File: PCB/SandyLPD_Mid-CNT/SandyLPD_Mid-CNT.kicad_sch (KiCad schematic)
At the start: 24 parts

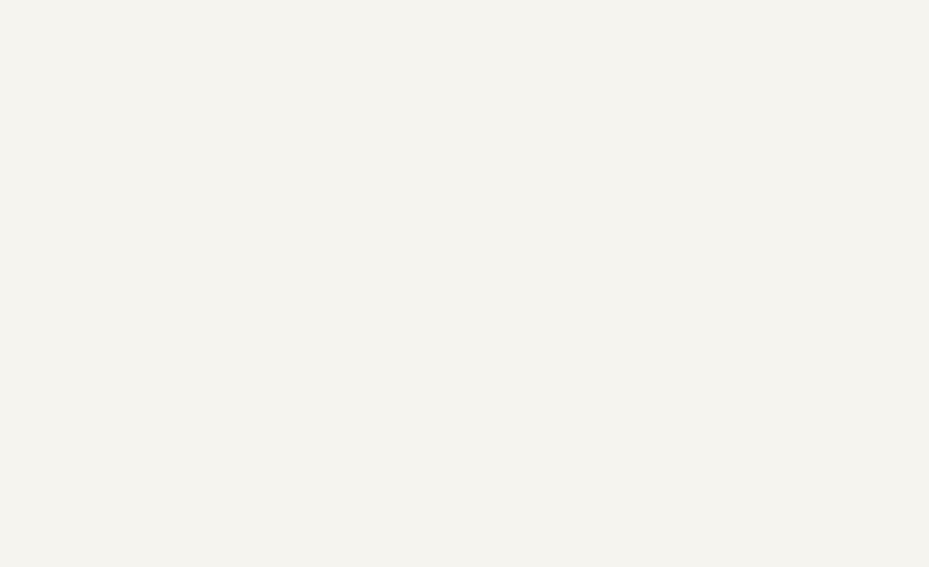
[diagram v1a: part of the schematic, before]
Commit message: Mid中央、配線やシルク調整中。
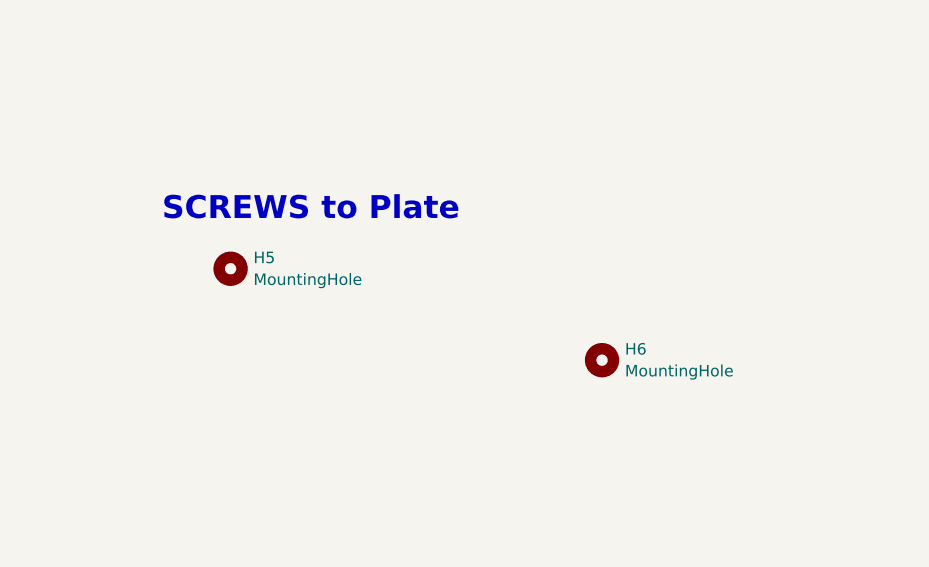
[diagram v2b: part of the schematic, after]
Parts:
- added H5, H6: MountingHole, locallib:MountingHole_M2_Through-hole_tap_THC-0.8-x-2, symbol Mechanical:MountingHole
- H1, H2, H3, H4: footprint locallib:MountingHole_1.8-2.2mm_M2_Pad_minimal -> locallib:MountingHole_2.2mm_M2_Pad_minimal
- SW_H1, SW_MACRO_R1, SW_U1: footprint locallib:Kailh_socket_ChocV2 -> locallib:Kailh_socket_ChocV2_for_Reverse
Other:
- note added: "SCREWS to Plate"
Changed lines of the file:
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@@
+		)
+	)
+	(text "SCREWS to Plate"
+		(exclude_from_sim no)
+		(at 37.465 248.92 0)
+		(effects
+			(font
+				(size 2.54 2.54)
+				(thickness 0.508)
+				(bold yes)
+			)
+			(justify left bottom)
 		)
 	)
@@
 			)
 		)
-		(property "Footprint" "locallib:MountingHole_1.8-2.2mm_M2_Pad_minimal"
+		(property "Footprint" "locallib:MountingHole_2.2mm_M2_Pad_minimal"
 			(at 78.105 203.835 0)
 			(effects
@@
 			)
 		)
-		(property "Footprint" "locallib:MountingHole_1.8-2.2mm_M2_Pad_minimal"
+		(property "Footprint" "locallib:MountingHole_2.2mm_M2_Pad_minimal"
 			(at 87.63 216.535 0)
 			(effects
@@
 			)
 		)
-		(property "Footprint" "locallib:MountingHole_1.8-2.2mm_M2_Pad_minimal"
+		(property "Footprint" "locallib:MountingHole_2.2mm_M2_Pad_minimal"
 			(at 40.64 177.8 0)
 			(effects
@@
 			)
 		)
-		(property "Footprint" "locallib:Kailh_socket_ChocV2"
+		(property "Footprint" "locallib:Kailh_socket_ChocV2_for_Reverse"
 			(at 158.75 74.295 0)
 			(effects
@@
 			)
 		)
-		(property "Footprint" "locallib:MountingHole_1.8-2.2mm_M2_Pad_minimal"
+		(property "Footprint" "locallib:MountingHole_2.2mm_M2_Pad_minimal"
 			(at 67.31 190.5 0)
 			(effects
@@
 				(path "/a99ab643-cdc7-4f8c-8088-c1f4faa914d1"
 					(reference "H2")
+					(unit 1)
+				)
+			)
+		)
+	)
+	(symbol
+		(lib_id "Mechanical:MountingHole")
+		(at 86.36 264.16 0)
+		(unit 1)
+		(exclude_from_sim yes)
+		(in_bom no)
+		(on_board yes)
+		(dnp no)
+		(fields_autoplaced yes)
+		(property "Reference" "H6"
+			(at 88.9 262.9478 0)
+			(effects
+				(font
+					(size 1.27 1.27)
+				)
+				(justify left)
+			)
+		)
+		(property "Value" "MountingHole"
+			(at 88.9 265.3721 0)
+			(effects
+				(font
+					(size 1.27 1.27)
+				)
+				(justify left)
+			)
+		)
+		(property "Footprint" "locallib:MountingHole_M2_Through-hole_tap_THC-0.8-x-2"
+			(at 86.36 264.16 0)
+			(effects
+				(font
+					(size 1.27 1.27)
+				)
+				(hide yes)
+			)
+		)
+		(property "Datasheet" "~"
+			(at 86.36 264.16 0)
+			(effects
+				(font
+					(size 1.27 1.27)
+				)
+				(hide yes)
+			)
+		)
+		(property "Description" "Mounting Hole without connection"
+			(at 86.36 264.16 0)
+			(effects
+				(font
+					(size 1.27 1.27)
+				)
+				(hide yes)
+			)
+		)
+		(instances
+			(project "SandyLPD_Mid-CNT"
+				(path "/a99ab643-cdc7-4f8c-8088-c1f4faa914d1"
+					(reference "H6")
+					(unit 1)
+				)
+			)
+		)
+	)
+	(symbol
+		(lib_id "Mechanical:MountingHole")
+		(at 45.085 254 0)
+		(unit 1)
+		(exclude_from_sim yes)
+		(in_bom no)
+		(on_board yes)
+		(dnp no)
+		(fields_autoplaced yes)
+		(property "Reference" "H5"
+			(at 47.625 252.7878 0)
+			(effects
+				(font
+					(size 1.27 1.27)
+				)
+				(justify left)
+			)
+		)
+		(property "Value" "MountingHole"
+			(at 47.625 255.2121 0)
+			(effects
+				(font
+					(size 1.27 1.27)
+				)
+				(justify left)
+			)
+		)
+		(property "Footprint" "locallib:MountingHole_M2_Through-hole_tap_THC-0.8-x-2"
+			(at 45.085 254 0)
+			(effects
+				(font
+					(size 1.27 1.27)
+				)
+				(hide yes)
+			)
+		)
+		(property "Datasheet" "~"
+			(at 45.085 254 0)
+			(effects
+				(font
+					(size 1.27 1.27)
+				)
+				(hide yes)
+			)
+		)
+		(property "Description" "Mounting Hole without connection"
+			(at 45.085 254 0)
+			(effects
+				(font
+					(size 1.27 1.27)
+				)
+				(hide yes)
+			)
+		)
+		(instances
+			(project ""
+				(path "/a99ab643-cdc7-4f8c-8088-c1f4faa914d1"
+					(reference "H5")
 					(unit 1)
 				)
@@
 			)
 		)
-		(property "Footprint" "locallib:Kailh_socket_ChocV2"
+		(property "Footprint" "locallib:Kailh_socket_ChocV2_for_Reverse"
 			(at 158.75 107.315 0)
 			(effects
@@
 			)
 		)
-		(property "Footprint" "locallib:Kailh_socket_ChocV2"
+		(property "Footprint" "locallib:Kailh_socket_ChocV2_for_Reverse"
 			(at 142.24 42.545 0)
 			(effects

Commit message: パーツ配置完了。ネジ位置調整中。
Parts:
- SW_G1, SW_MACRO_L1, SW_R1: footprint locallib:Kailh_socket_ChocV2_small_#2pad -> locallib:Kailh_socket_ChocV2_small_#2pad_for_Reverse_no_hole
- renumbered D3 to D1, D1 to D2, D7 to D3, D2 to D4, D12 to D5, D4 to D6, T_R0 to T_R1, T_R1 to T_R2, T_R2 to T_R3
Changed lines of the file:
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@@
 		(on_board yes)
 		(dnp no)
-		(property "Reference" "D3"
+		(property "Reference" "D1"
 			(at 47.117 50.2666 90)
 			(effects
@@
 			(project "Sandy_Middle"
 				(path "/a99ab643-cdc7-4f8c-8088-c1f4faa914d1"
-					(reference "D3")
+					(reference "D1")
 					(unit 1)
 				)
@@
 		(on_board yes)
 		(dnp no)
-		(property "Reference" "T_R0"
+		(property "Reference" "T_R1"
 			(at 94.107 55.4482 0)
 			(effects
@@
 			(project "Sandy_Middle"
 				(path "/a99ab643-cdc7-4f8c-8088-c1f4faa914d1"
-					(reference "T_R0")
+					(reference "T_R1")
 					(unit 1)
 				)
@@
 			)
 		)
-		(property "Footprint" "locallib:Kailh_socket_ChocV2_small_#2pad"
+		(property "Footprint" "locallib:Kailh_socket_ChocV2_small_#2pad_for_Reverse_no_hole"
 			(at 40.005 42.545 0)
 			(effects
@@
 		(on_board yes)
 		(dnp no)
-		(property "Reference" "D1"
+		(property "Reference" "D2"
 			(at 149.352 50.2666 90)
 			(effects
@@
 			(project "SandyLPD_Mid-CNT"
 				(path "/a99ab643-cdc7-4f8c-8088-c1f4faa914d1"
-					(reference "D1")
+					(reference "D2")
 					(unit 1)
 				)
@@
 		(on_board yes)
 		(dnp no)
-		(property "Reference" "D4"
+		(property "Reference" "D6"
 			(at 165.862 115.0366 90)
 			(effects
@@
 			(project "SandyLPD_Mid-CNT"
 				(path "/a99ab643-cdc7-4f8c-8088-c1f4faa914d1"
-					(reference "D4")
+					(reference "D6")
 					(unit 1)
 				)
@@
 		(on_board yes)
 		(dnp no)
-		(property "Reference" "D7"
+		(property "Reference" "D3"
 			(at 63.627 82.0166 90)
 			(effects
@@
 			(project "Sandy_Middle"
 				(path "/a99ab643-cdc7-4f8c-8088-c1f4faa914d1"
-					(reference "D7")
+					(reference "D3")
 					(unit 1)
 				)
@@
 		(on_board yes)
 		(dnp no)
-		(property "Reference" "T_R2"
+		(property "Reference" "T_R3"
 			(at 94.107 118.9482 0)
 			(effects
@@
 			(project "Sandy_Middle"
 				(path "/a99ab643-cdc7-4f8c-8088-c1f4faa914d1"
-					(reference "T_R2")
+					(reference "T_R3")
 					(unit 1)
 				)
@@
 		(on_board yes)
 		(dnp no)
-		(property "Reference" "T_R1"
+		(property "Reference" "T_R2"
 			(at 94.107 89.7382 0)
 			(effects
@@
 			(project "Sandy_Middle"
 				(path "/a99ab643-cdc7-4f8c-8088-c1f4faa914d1"
-					(reference "T_R1")
+					(reference "T_R2")
 					(unit 1)
 				)
@@
 		(on_board yes)
 		(dnp no)
-		(property "Reference" "D2"
+		(property "Reference" "D4"
 			(at 165.862 82.0166 90)
 			(effects
@@
 			(project "SandyLPD_Mid-CNT"
 				(path "/a99ab643-cdc7-4f8c-8088-c1f4faa914d1"
-					(reference "D2")
+					(reference "D4")
 					(unit 1)
 				)
@@
 			)
 		)
-		(property "Footprint" "locallib:Kailh_socket_ChocV2_small_#2pad"
+		(property "Footprint" "locallib:Kailh_socket_ChocV2_small_#2pad_for_Reverse_no_hole"
 			(at 56.515 74.295 0)
 			(effects
@@
 		(on_board yes)
 		(dnp no)
-		(property "Reference" "D12"
+		(property "Reference" "D5"
 			(at 63.627 115.0366 90)
 			(effects
@@
 			(project "Sandy_Middle"
 				(path "/a99ab643-cdc7-4f8c-8088-c1f4faa914d1"
-					(reference "D12")
+					(reference "D5")
 					(unit 1)
 				)
@@
 			)
 		)
-		(property "Footprint" "locallib:Kailh_socket_ChocV2_small_#2pad"
+		(property "Footprint" "locallib:Kailh_socket_ChocV2_small_#2pad_for_Reverse_no_hole"
 			(at 56.515 107.315 0)
 			(effects

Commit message: スルーホールタップの接続先を変更・調整 #19
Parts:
- H1, H2, H3, H4, H_top_1, H_top_2, H_top_3: footprint locallib:MountingHole_2.2mm_M2_Pad_minimal -> locallib:MountingHole_2.2-4.8mm_M2_Pad_minimal_for_Through-hole_tap
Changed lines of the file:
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@@
 			)
 		)
-		(property "Footprint" "locallib:MountingHole_2.2mm_M2_Pad_minimal"
+		(property "Footprint" "locallib:MountingHole_2.2-4.8mm_M2_Pad_minimal_for_Through-hole_tap"
 			(at 78.105 203.835 0)
 			(effects
@@
 			)
 		)
-		(property "Footprint" "locallib:MountingHole_2.2mm_M2_Pad_minimal"
+		(property "Footprint" "locallib:MountingHole_2.2-4.8mm_M2_Pad_minimal_for_Through-hole_tap"
 			(at 157.48 193.04 0)
 			(effects
@@
 			)
 		)
-		(property "Footprint" "locallib:MountingHole_2.2mm_M2_Pad_minimal"
+		(property "Footprint" "locallib:MountingHole_2.2-4.8mm_M2_Pad_minimal_for_Through-hole_tap"
 			(at 87.63 216.535 0)
 			(effects
@@
 			)
 		)
-		(property "Footprint" "locallib:MountingHole_2.2mm_M2_Pad_minimal"
+		(property "Footprint" "locallib:MountingHole_2.2-4.8mm_M2_Pad_minimal_for_Through-hole_tap"
 			(at 40.64 177.8 0)
 			(effects
@@
 			)
 		)
-		(property "Footprint" "locallib:MountingHole_2.2mm_M2_Pad_minimal"
+		(property "Footprint" "locallib:MountingHole_2.2-4.8mm_M2_Pad_minimal_for_Through-hole_tap"
 			(at 133.985 177.8 0)
 			(effects
@@
 			)
 		)
-		(property "Footprint" "locallib:MountingHole_2.2mm_M2_Pad_minimal"
+		(property "Footprint" "locallib:MountingHole_2.2-4.8mm_M2_Pad_minimal_for_Through-hole_tap"
 			(at 67.31 190.5 0)
 			(effects
@@
 			)
 		)
-		(property "Footprint" "locallib:MountingHole_2.2mm_M2_Pad_minimal"
+		(property "Footprint" "locallib:MountingHole_2.2-4.8mm_M2_Pad_minimal_for_Through-hole_tap"
 			(at 157.48 177.8 0)
 			(effects

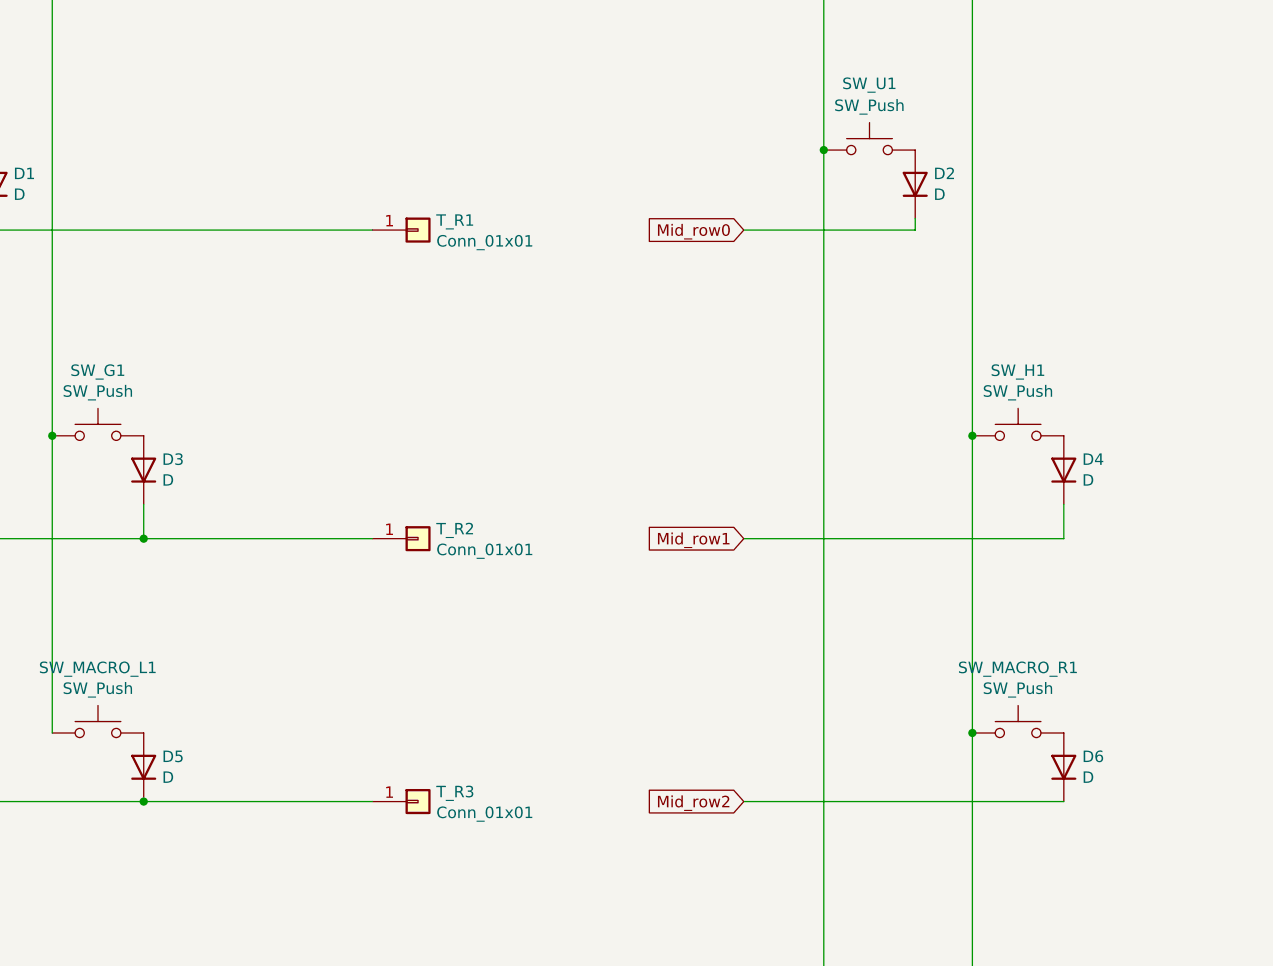
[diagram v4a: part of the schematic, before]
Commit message: ダイオードの番号を調整
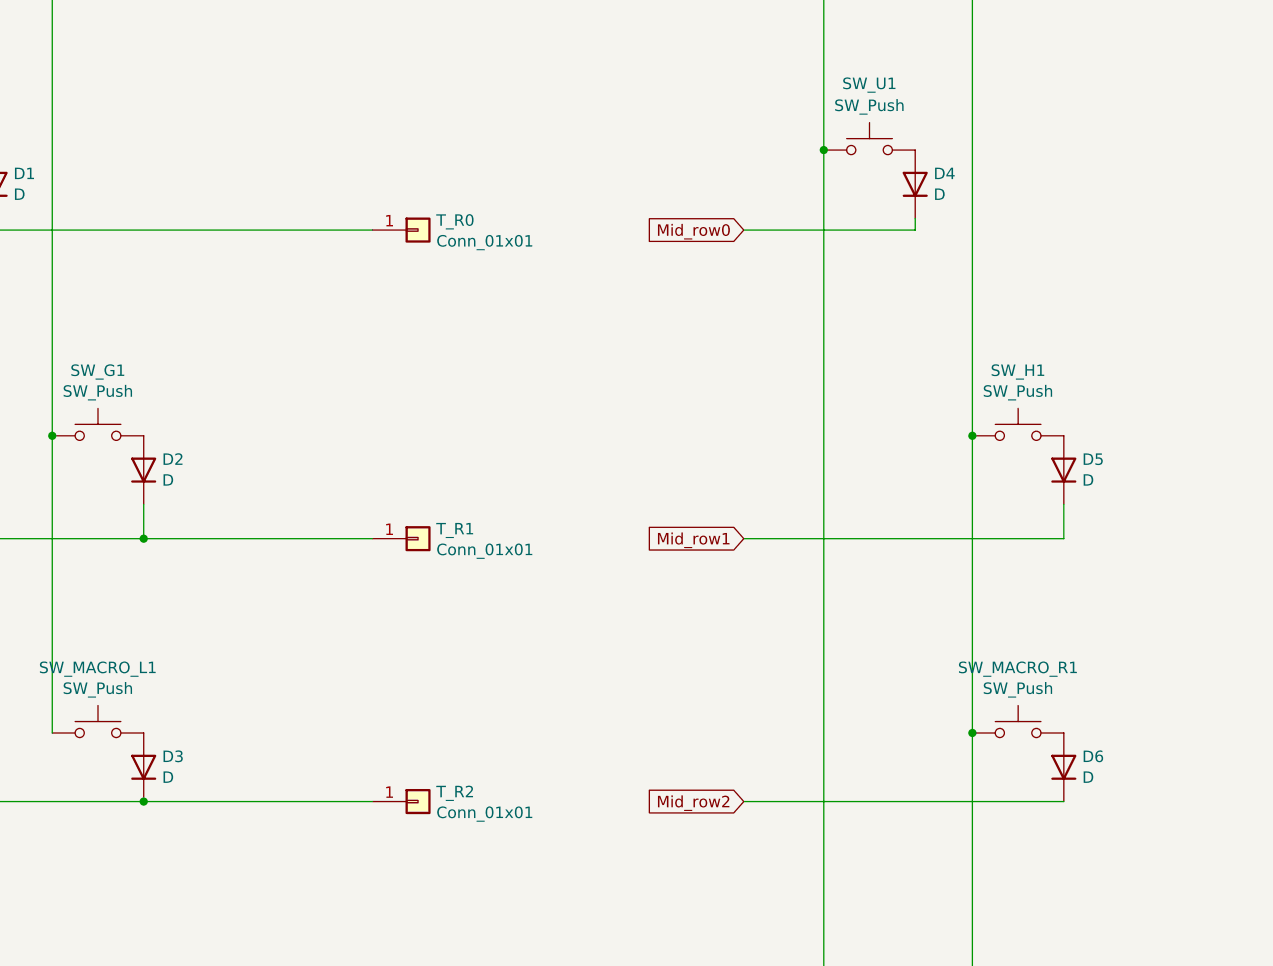
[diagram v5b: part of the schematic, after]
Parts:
- renumbered D3 to D2, D5 to D3, D2 to D4, D4 to D5, T_R1 to T_R0, T_R2 to T_R1, T_R3 to T_R2
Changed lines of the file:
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@@
 		(on_board yes)
 		(dnp no)
-		(property "Reference" "T_R1"
+		(property "Reference" "T_R0"
 			(at 94.107 55.4482 0)
 			(effects
@@
 			(project "Sandy_Middle"
 				(path "/a99ab643-cdc7-4f8c-8088-c1f4faa914d1"
-					(reference "T_R1")
+					(reference "T_R0")
 					(unit 1)
 				)
@@
 		(on_board yes)
 		(dnp no)
-		(property "Reference" "D2"
+		(property "Reference" "D4"
 			(at 149.352 50.2666 90)
 			(effects
@@
 			(project "SandyLPD_Mid-CNT"
 				(path "/a99ab643-cdc7-4f8c-8088-c1f4faa914d1"
-					(reference "D2")
+					(reference "D4")
 					(unit 1)
 				)
@@
 		(on_board yes)
 		(dnp no)
-		(property "Reference" "D3"
+		(property "Reference" "D2"
 			(at 63.627 82.0166 90)
 			(effects
@@
 			(project "Sandy_Middle"
 				(path "/a99ab643-cdc7-4f8c-8088-c1f4faa914d1"
-					(reference "D3")
+					(reference "D2")
 					(unit 1)
 				)
@@
 		(on_board yes)
 		(dnp no)
-		(property "Reference" "T_R3"
+		(property "Reference" "T_R2"
 			(at 94.107 118.9482 0)
 			(effects
@@
 			(project "Sandy_Middle"
 				(path "/a99ab643-cdc7-4f8c-8088-c1f4faa914d1"
-					(reference "T_R3")
+					(reference "T_R2")
 					(unit 1)
 				)
@@
 		(on_board yes)
 		(dnp no)
-		(property "Reference" "T_R2"
+		(property "Reference" "T_R1"
 			(at 94.107 89.7382 0)
 			(effects
@@
 			(project "Sandy_Middle"
 				(path "/a99ab643-cdc7-4f8c-8088-c1f4faa914d1"
-					(reference "T_R2")
+					(reference "T_R1")
 					(unit 1)
 				)
@@
 		(on_board yes)
 		(dnp no)
-		(property "Reference" "D4"
+		(property "Reference" "D5"
 			(at 165.862 82.0166 90)
 			(effects
@@
 			(project "SandyLPD_Mid-CNT"
 				(path "/a99ab643-cdc7-4f8c-8088-c1f4faa914d1"
-					(reference "D4")
+					(reference "D5")
 					(unit 1)
 				)
@@
 		(on_board yes)
 		(dnp no)
-		(property "Reference" "D5"
+		(property "Reference" "D3"
 			(at 63.627 115.0366 90)
 			(effects
@@
 			(project "Sandy_Middle"
 				(path "/a99ab643-cdc7-4f8c-8088-c1f4faa914d1"
-					(reference "D5")
-					(unit 1)
-				)
+					(reference "D3")
+					(unit 1)
+				)

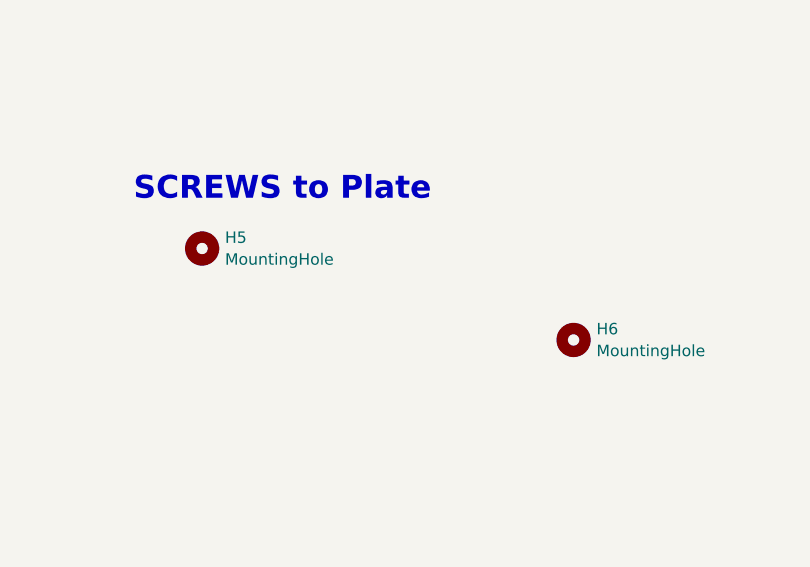
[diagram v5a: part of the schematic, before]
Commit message: Mid-CNTのプレート固定用スルーホールタップを1個減らす
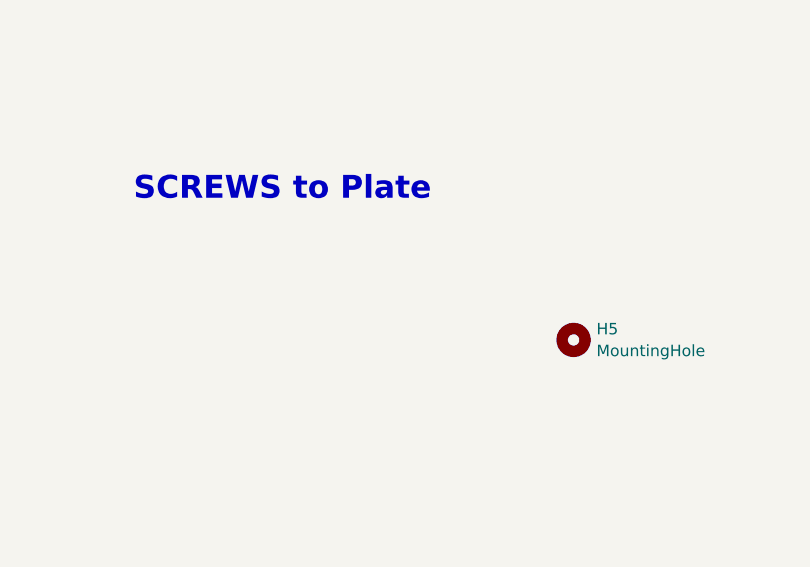
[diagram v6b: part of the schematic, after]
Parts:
- removed H5: MountingHole, locallib:MountingHole_M2_Through-hole_tap_THC-0.8-x-2, symbol Mechanical:MountingHole
- renumbered H6 to H5
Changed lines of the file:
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@@
 		(dnp no)
 		(fields_autoplaced yes)
-		(property "Reference" "H6"
+		(property "Reference" "H5"
 			(at 88.9 262.9478 0)
 			(effects
@@
 			(project "SandyLPD_Mid-CNT"
 				(path "/a99ab643-cdc7-4f8c-8088-c1f4faa914d1"
-					(reference "H6")
-					(unit 1)
-				)
-			)
-		)
-	)
-	(symbol
-		(lib_id "Mechanical:MountingHole")
-		(at 45.085 254 0)
-		(unit 1)
-		(exclude_from_sim yes)
-		(in_bom no)
-		(on_board yes)
-		(dnp no)
-		(fields_autoplaced yes)
-		(property "Reference" "H5"
-			(at 47.625 252.7878 0)
-			(effects
-				(font
-					(size 1.27 1.27)
-				)
-				(justify left)
-			)
-		)
-		(property "Value" "MountingHole"
-			(at 47.625 255.2121 0)
-			(effects
-				(font
-					(size 1.27 1.27)
-				)
-				(justify left)
-			)
-		)
-		(property "Footprint" "locallib:MountingHole_M2_Through-hole_tap_THC-0.8-x-2"
-			(at 45.085 254 0)
-			(effects
-				(font
-					(size 1.27 1.27)
-				)
-				(hide yes)
-			)
-		)
-		(property "Datasheet" "~"
-			(at 45.085 254 0)
-			(effects
-				(font
-					(size 1.27 1.27)
-				)
-				(hide yes)
-			)
-		)
-		(property "Description" "Mounting Hole without connection"
-			(at 45.085 254 0)
-			(effects
-				(font
-					(size 1.27 1.27)
-				)
-				(hide yes)
-			)
-		)
-		(instances
-			(project ""
-				(path "/a99ab643-cdc7-4f8c-8088-c1f4faa914d1"
 					(reference "H5")
